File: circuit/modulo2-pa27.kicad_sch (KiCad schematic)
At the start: 47 parts, among them J2 CONN_01X04, J3 CONN_01X04, J4 JACK_MONO, J5 HOLE, J7 HOLE, SW1 bright, U1 OPA2134, U2 OPA2134, U3 TLE2426

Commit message: further routing
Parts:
- C10, C4: footprint myAmp:C_FILM_L7.2mm_W3.5mm_P5.00mm -> myAmp:C_2.5MM
- C22, C23: footprint myAmp:C_1206 -> myAmp:C_5MM_1206
- C5: value 1n -> 250p
- C6: value 220n -> 100n
- C7: value 100n -> 47n
- R8: value 33k -> 100k
- RV1, RV2: value 50k -> 250k
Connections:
- net TRB: now also C5.2, RV1.3; no longer RV1.2, RV4.3
- new net: RV1.2, RV4.3
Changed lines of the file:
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@@
     (effects (font (size 1.27 1.27)) (justify left bottom))
   )
-  (label "TRB" (at 134.62 41.91 0)
+  (label "TRB" (at 123.19 34.29 0)
     (effects (font (size 1.27 1.27)) (justify left bottom))
   )
@@
     (property "Reference" "C22" (id 0) (at 16.51 69.85 0))
     (property "Value" "100nF" (id 1) (at 15.24 64.77 0))
-    (property "Footprint" "myAmp:C_1206" (id 2) (at 18.0848 63.5 0)
+    (property "Footprint" "myAmp:C_5MM_1206" (id 2) (at 18.0848 63.5 0)
       (effects (font (size 1.27 1.27)) hide)
     )
@@
       (effects (font (size 1.27 1.27)) (justify right))
     )
-    (property "Value" "50k" (id 1) (at 125.222 43.053 0)
+    (property "Value" "250k" (id 1) (at 125.222 43.053 0)
       (effects (font (size 1.27 1.27)) (justify right))
     )
@@
       (effects (font (size 1.27 1.27)) (justify right))
     )
-    (property "Value" "50k" (id 1) (at 125.222 58.293 0)
+    (property "Value" "250k" (id 1) (at 125.222 58.293 0)
       (effects (font (size 1.27 1.27)) (justify right))
     )
@@
     (in_bom yes) (on_board yes)
     (property "Reference" "C5" (id 0) (at 118.11 30.48 90))
-    (property "Value" "1n" (id 1) (at 118.11 38.1 90))
+    (property "Value" "250p" (id 1) (at 118.11 38.1 90))
     (property "Footprint" "myAmp:C_FILM_L7.2mm_W3.5mm_P5.00mm" (id 2) (at 121.92 33.3248 0)
       (effects (font (size 1.27 1.27)) hide)
@@
       (effects (font (size 1.27 1.27)) (justify right))
     )
-    (property "Value" "33k" (id 1) (at 110.49 43.18 0)
+    (property "Value" "100k" (id 1) (at 110.49 43.18 0)
       (effects (font (size 1.27 1.27)) (justify right))
     )
@@
   (symbol (lib_id "myAmp:C") (at 118.11 49.53 90) (unit 1)
     (in_bom yes) (on_board yes)
-    (property "Reference" "C6" (id 0) (at 118.11 46.99 90))
-    (property "Value" "220n" (id 1) (at 118.11 53.34 90))
+    (property "Reference" "C6" (id 0) (at 118.11 45.72 90))
+    (property "Value" "100n" (id 1) (at 118.11 53.34 90))
     (property "Footprint" "myAmp:C_FILM_L7.2mm_W3.5mm_P5.00mm" (id 2) (at 121.92 48.5648 0)
       (effects (font (size 1.27 1.27)) hide)
@@
   (symbol (lib_id "myAmp:C") (at 118.11 63.5 90) (unit 1)
     (in_bom yes) (on_board yes)
-    (property "Reference" "C7" (id 0) (at 118.11 60.96 90))
-    (property "Value" "100n" (id 1) (at 118.11 67.31 90))
+    (property "Reference" "C7" (id 0) (at 118.11 59.69 90))
+    (property "Value" "47n" (id 1) (at 118.11 67.31 90))
     (property "Footprint" "myAmp:C_FILM_L7.2mm_W3.5mm_P5.00mm" (id 2) (at 121.92 62.5348 0)
       (effects (font (size 1.27 1.27)) hide)
@@
     (property "Reference" "C10" (id 0) (at 179.07 53.34 90))
     (property "Value" "120p" (id 1) (at 179.07 60.96 90))
-    (property "Footprint" "myAmp:C_FILM_L7.2mm_W3.5mm_P5.00mm" (id 2) (at 182.88 56.1848 0)
+    (property "Footprint" "myAmp:C_2.5MM" (id 2) (at 182.88 56.1848 0)
       (effects (font (size 1.27 1.27)) hide)
     )
@@
     (property "Reference" "C4" (id 0) (at 99.06 53.34 90))
     (property "Value" "120p" (id 1) (at 99.06 60.96 90))
-    (property "Footprint" "myAmp:C_FILM_L7.2mm_W3.5mm_P5.00mm" (id 2) (at 102.87 56.1848 0)
+    (property "Footprint" "myAmp:C_2.5MM" (id 2) (at 102.87 56.1848 0)
       (effects (font (size 1.27 1.27)) hide)
     )
@@
     (property "Reference" "C23" (id 0) (at 36.83 69.85 0))
     (property "Value" "100nF" (id 1) (at 35.56 64.77 0))
-    (property "Footprint" "myAmp:C_1206" (id 2) (at 38.4048 63.5 0)
+    (property "Footprint" "myAmp:C_5MM_1206" (id 2) (at 38.4048 63.5 0)
       (effects (font (size 1.27 1.27)) hide)
     )
@@
     )
     (path "/48142eaa-7210-4390-91e8-e59685a2b4d4"
-      (reference "C4") (unit 1) (value "120p") (footprint "myAmp:C_FILM_L7.2mm_W3.5mm_P5.00mm")
+      (reference "C4") (unit 1) (value "120p") (footprint "myAmp:C_2.5MM")
     )
     (path "/00000000-0000-0000-0000-000061c307c0"
-      (reference "C5") (unit 1) (value "1n") (footprint "myAmp:C_FILM_L7.2mm_W3.5mm_P5.00mm")
+      (reference "C5") (unit 1) (value "250p") (footprint "myAmp:C_FILM_L7.2mm_W3.5mm_P5.00mm")
     )
     (path "/00000000-0000-0000-0000-000061c52359"
-      (reference "C6") (unit 1) (value "220n") (footprint "myAmp:C_FILM_L7.2mm_W3.5mm_P5.00mm")
+      (reference "C6") (unit 1) (value "100n") (footprint "myAmp:C_FILM_L7.2mm_W3.5mm_P5.00mm")
     )
     (path "/00000000-0000-0000-0000-000061c52e5e"
-      (reference "C7") (unit 1) (value "100n") (footprint "myAmp:C_FILM_L7.2mm_W3.5mm_P5.00mm")
+      (reference "C7") (unit 1) (value "47n") (footprint "myAmp:C_FILM_L7.2mm_W3.5mm_P5.00mm")
     )
     (path "/11af6226-d94c-469b-95d8-d952d2567f76"
@@
     )
     (path "/1c4bff62-038b-4006-b722-9d6b6553e13a"
-      (reference "C10") (unit 1) (value "120p") (footprint "myAmp:C_FILM_L7.2mm_W3.5mm_P5.00mm")
+      (reference "C10") (unit 1) (value "120p") (footprint "myAmp:C_2.5MM")
     )
     (path "/70af284c-9682-4272-9658-52b4c38f7d80"
@@
     )
     (path "/00000000-0000-0000-0000-00005f0669ed"
-      (reference "C22") (unit 1) (value "100nF") (footprint "myAmp:C_1206")
+      (reference "C22") (unit 1) (value "100nF") (footprint "myAmp:C_5MM_1206")
     )
     (path "/fb1c6638-be6b-421d-993a-23927fb374fb"
-      (reference "C23") (unit 1) (value "100nF") (footprint "myAmp:C_1206")
+      (reference "C23") (unit 1) (value "100nF") (footprint "myAmp:C_5MM_1206")
     )
     (path "/00000000-0000-0000-0000-000061b9e69a"
@@
     )
     (path "/00000000-0000-0000-0000-000061c471ae"
-      (reference "R8") (unit 1) (value "33k") (footprint "myAmp:R_10MM")
+      (reference "R8") (unit 1) (value "100k") (footprint "myAmp:R_10MM")
     )
     (path "/844c38d0-9f18-4b6e-9f2e-f1c5539e0fd4"
@@
     )
     (path "/00000000-0000-0000-0000-000061c2ed9a"
-      (reference "RV1") (unit 1) (value "50k") (footprint "myAmp:BOURNS_PTD901_xx15K")
+      (reference "RV1") (unit 1) (value "250k") (footprint "myAmp:BOURNS_PTD901_xx15K")
     )
     (path "/00000000-0000-0000-0000-000061c2f7c7"
-      (reference "RV2") (unit 1) (value "50k") (footprint "myAmp:BOURNS_PTD901_xx15K")
+      (reference "RV2") (unit 1) (value "250k") (footprint "myAmp:BOURNS_PTD901_xx15K")
     )
     (path "/00000000-0000-0000-0000-000061c300fc"

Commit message: redone layout and tracing
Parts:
- added C24, C25: 47u, myAmp:CPOL_D6.3_P2.5, symbol myAmp:CPOL
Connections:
- net +24V: now also C24.1, C25.1
- net GND: now also C24.2, C25.2
- net PA_OUT: now also J3.2 (P2), J3.4; no longer J3.1 (P1), J3.3
- net VGND: now also J3.1 (P1), J3.3; no longer J3.2 (P2), J3.4
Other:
- moved on the sheet: J3
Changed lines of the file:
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@@
   (junction (at 109.22 34.29) (diameter 0) (color 0 0 0 0)
   )
+  (junction (at 102.87 102.87) (diameter 0) (color 0 0 0 0)
+  )
   (junction (at 44.45 57.15) (diameter 0) (color 0 0 0 0)
   )
   (junction (at 127 63.5) (diameter 0) (color 0 0 0 0)
+  )
+  (junction (at 78.74 176.53) (diameter 0) (color 0 0 0 0)
   )
   (junction (at 161.29 48.26) (diameter 0) (color 0 0 0 0)
@@
     (stroke (width 0) (type default) (color 0 0 0 0))
   )
-  (wire (pts (xy 50.8 182.88) (xy 58.42 182.88))
+  (wire (pts (xy 50.8 172.72) (xy 58.42 172.72))
     (stroke (width 0) (type default) (color 0 0 0 0))
   )
@@
     (stroke (width 0) (type default) (color 0 0 0 0))
   )
+  (wire (pts (xy 78.74 182.88) (xy 78.74 185.42))
+    (stroke (width 0) (type default) (color 0 0 0 0))
+  )
   (wire (pts (xy 200.66 54.61) (xy 200.66 59.69))
     (stroke (width 0) (type default) (color 0 0 0 0))
@@
     (stroke (width 0) (type default) (color 0 0 0 0))
   )
+  (wire (pts (xy 102.87 102.87) (xy 102.87 105.41))
+    (stroke (width 0) (type default) (color 0 0 0 0))
+  )
   (wire (pts (xy 184.15 57.15) (xy 181.61 57.15))
     (stroke (width 0) (type default) (color 0 0 0 0))
@@
     (stroke (width 0) (type default) (color 0 0 0 0))
   )
+  (wire (pts (xy 78.74 176.53) (xy 78.74 177.8))
+    (stroke (width 0) (type default) (color 0 0 0 0))
+  )
   (wire (pts (xy 80.01 44.45) (xy 82.55 44.45))
     (stroke (width 0) (type default) (color 0 0 0 0))
@@
   )
   (wire (pts (xy 193.04 54.61) (xy 200.66 54.61))
+    (stroke (width 0) (type default) (color 0 0 0 0))
+  )
+  (wire (pts (xy 102.87 110.49) (xy 102.87 114.3))
     (stroke (width 0) (type default) (color 0 0 0 0))
   )
@@
     (effects (font (size 1.27 1.27)) (justify left bottom))
   )
-  (label "VGND" (at 50.8 182.88 0)
+  (label "VGND" (at 50.8 172.72 0)
     (effects (font (size 1.27 1.27)) (justify left bottom))
   )
@@
     (pin "1")
   )
-  (symbol (lib_id "myAmp:CONN_01X04") (at 63.5 179.07 0) (unit 1)
-    (in_bom yes) (on_board yes)
-    (property "Reference" "J3" (id 0) (at 65.4812 179.197 0)
+  (symbol (lib_id "myAmp:CONN_01X04") (at 63.5 176.53 0) (unit 1)
+    (in_bom yes) (on_board yes)
+    (property "Reference" "J3" (id 0) (at 65.4812 176.657 0)
       (effects (font (size 1.27 1.27)) (justify left))
     )
-    (property "Value" "CONN_01X04" (id 1) (at 66.04 179.07 90)
-      (effects (font (size 1.27 1.27)) hide)
-    )
-    (property "Footprint" "myAmp:PIN_1x04" (id 2) (at 63.5 179.07 0)
-      (effects (font (size 1.27 1.27)) hide)
-    )
-    (property "Datasheet" "" (id 3) (at 63.5 179.07 0)
+    (property "Value" "CONN_01X04" (id 1) (at 66.04 176.53 90)
+      (effects (font (size 1.27 1.27)) hide)
+    )
+    (property "Footprint" "myAmp:PIN_1x04" (id 2) (at 63.5 176.53 0)
+      (effects (font (size 1.27 1.27)) hide)
+    )
+    (property "Datasheet" "" (id 3) (at 63.5 176.53 0)
       (effects (font (size 1.27 1.27)) hide)
     )
@@
     (pin "2")
   )
+  (symbol (lib_id "myAmp:CPOL") (at 78.74 180.34 0) (unit 1)
+    (in_bom yes) (on_board yes) (fields_autoplaced)
+    (property "Reference" "C24" (id 0) (at 81.28 178.5238 0)
+      (effects (font (size 1.27 1.27)) (justify left))
+    )
+    (property "Value" "47u" (id 1) (at 81.28 181.0638 0)
+      (effects (font (size 1.27 1.27)) (justify left))
+    )
+    (property "Footprint" "myAmp:CPOL_D6.3_P2.5" (id 2) (at 78.74 180.34 0)
+      (effects (font (size 1.27 1.27)) hide)
+    )
+    (property "Datasheet" "" (id 3) (at 78.74 180.34 0)
+      (effects (font (size 1.27 1.27)) hide)
+    )
+    (pin "1")
+    (pin "2")
+  )
   (symbol (lib_id "myAmp:C") (at 179.07 57.15 90) (unit 1)
     (in_bom yes) (on_board yes)
@@
     (pin "2")
   )
+  (symbol (lib_id "power:GND") (at 102.87 114.3 0) (unit 1)
+    (in_bom yes) (on_board yes)
+    (property "Reference" "#PWR0101" (id 0) (at 102.87 120.65 0)
+      (effects (font (size 1.27 1.27)) hide)
+    )
+    (property "Value" "GND" (id 1) (at 102.997 118.6942 0))
+    (property "Footprint" "" (id 2) (at 102.87 114.3 0)
+      (effects (font (size 1.27 1.27)) hide)
+    )
+    (property "Datasheet" "" (id 3) (at 102.87 114.3 0)
+      (effects (font (size 1.27 1.27)) hide)
+    )
+    (pin "1")
+  )
   (symbol (lib_id "myAmp:R") (at 236.22 63.5 180) (unit 1)
     (in_bom yes) (on_board yes)
@@
     (pin "1")
     (pin "2")
+  )
+  (symbol (lib_id "power:GND") (at 78.74 185.42 0) (mirror y) (unit 1)
+    (in_bom yes) (on_board yes)
+    (property "Reference" "#PWR03" (id 0) (at 78.74 191.77 0)
+      (effects (font (size 1.27 1.27)) hide)
+    )
+    (property "Value" "GND" (id 1) (at 78.613 189.8142 0))
+    (property "Footprint" "" (id 2) (at 78.74 185.42 0)
+      (effects (font (size 1.27 1.27)) hide)
+    )
+    (property "Datasheet" "" (id 3) (at 78.74 185.42 0)
+      (effects (font (size 1.27 1.27)) hide)
+    )
+    (pin "1")
   )
   (symbol (lib_id "myAmp:OPAMP") (at 250.19 39.37 0) (unit 2)
@@
     (pin "3")
   )
+  (symbol (lib_id "myAmp:CPOL") (at 102.87 107.95 0) (unit 1)
+    (in_bom yes) (on_board yes) (fields_autoplaced)
+    (property "Reference" "C25" (id 0) (at 105.41 106.1338 0)
+      (effects (font (size 1.27 1.27)) (justify left))
+    )
+    (property "Value" "47u" (id 1) (at 105.41 108.6738 0)
+      (effects (font (size 1.27 1.27)) (justify left))
+    )
+    (property "Footprint" "myAmp:CPOL_D6.3_P2.5" (id 2) (at 102.87 107.95 0)
+      (effects (font (size 1.27 1.27)) hide)
+    )
+    (property "Datasheet" "" (id 3) (at 102.87 107.95 0)
+      (effects (font (size 1.27 1.27)) hide)
+    )
+    (pin "1")
+    (pin "2")
+  )
   (symbol (lib_id "myAmp:R") (at 241.3 63.5 0) (mirror x) (unit 1)
     (in_bom yes) (on_board yes)
@@
       (reference "#PWR02") (unit 1) (value "+24V") (footprint "")
     )
+    (path "/90800a4d-a014-4b9a-947e-f975697802ee"
+      (reference "#PWR03") (unit 1) (value "GND") (footprint "")
+    )
     (path "/00000000-0000-0000-0000-00005f0669e6"
       (reference "#PWR05") (unit 1) (value "GND") (footprint "")
@@
       (reference "#PWR012") (unit 1) (value "GND") (footprint "")
     )
+    (path "/84916f83-d8a0-446a-8998-d523c09d50ab"
+      (reference "#PWR0101") (unit 1) (value "GND") (footprint "")
+    )
     (path "/00000000-0000-0000-0000-000061baa65d"
       (reference "C1") (unit 1) (value "47nF") (footprint "myAmp:C_FILM_L7.2mm_W3.5mm_P5.00mm")
@@
       (reference "C23") (unit 1) (value "100nF") (footprint "myAmp:C_5MM_1206")
     )
+    (path "/193e6f89-e90a-407b-9332-2aace38b0407"
+      (reference "C24") (unit 1) (value "47u") (footprint "myAmp:CPOL_D6.3_P2.5")
+    )
+    (path "/bec0516f-9815-4d8e-ba32-5bcb5afe996f"
+      (reference "C25") (unit 1) (value "47u") (footprint "myAmp:CPOL_D6.3_P2.5")
+    )
     (path "/00000000-0000-0000-0000-000061b9e69a"

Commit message: made a toner transfer pa27
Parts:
- RV4: footprint myAmp:BOURNS_PTD901_xx15K -> myAmp:POT_VULGARIS
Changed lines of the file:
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@@
       (effects (font (size 1.27 1.27)) (justify right))
     )
-    (property "Footprint" "myAmp:BOURNS_PTD901_xx15K" (id 2) (at 144.78 48.26 0)
+    (property "Footprint" "myAmp:POT_VULGARIS" (id 2) (at 144.78 48.26 0)
       (effects (font (size 1.27 1.27)) hide)
     )
@@
     )
     (path "/3815e89f-ae0b-444f-8039-7f1b98ab98ab"
-      (reference "RV4") (unit 1) (value "500k") (footprint "myAmp:BOURNS_PTD901_xx15K")
+      (reference "RV4") (unit 1) (value "500k") (footprint "myAmp:POT_VULGARIS")
     )
     (path "/77415905-9ad6-47f9-b33e-2e8f06373b35"

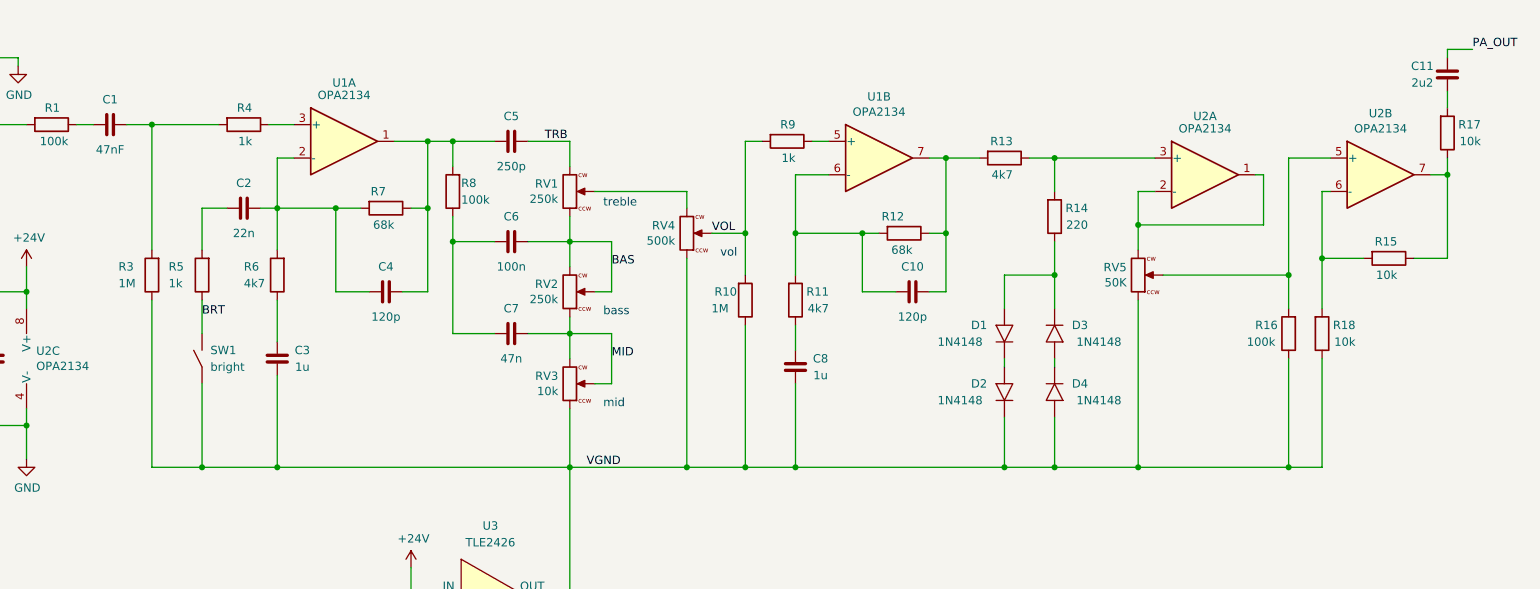
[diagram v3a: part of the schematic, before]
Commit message: made FV-1 prototype; converted kicad 5 files to kicad 6
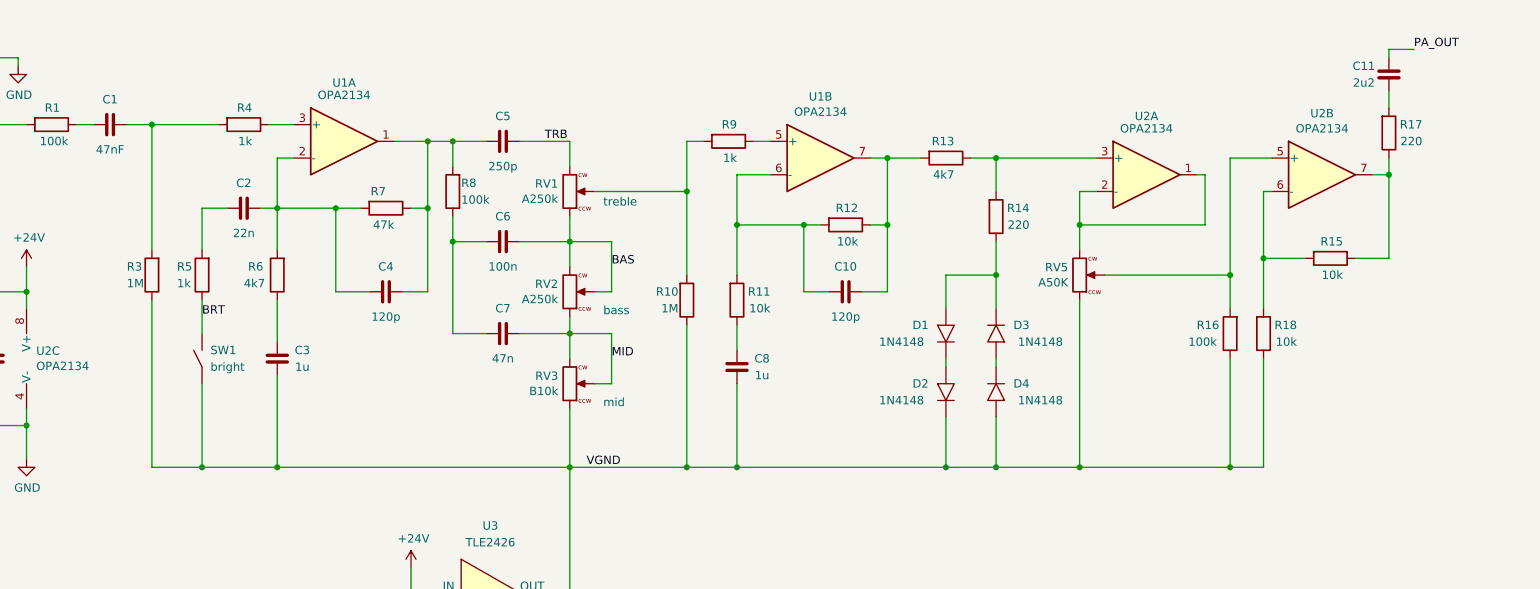
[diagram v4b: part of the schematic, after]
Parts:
- removed RV4: 500k, myAmp:POT_VULGARIS, symbol myAmp:R_POT
- R11: value 4k7 -> 10k
- R12: value 68k -> 10k
- R17: value 10k -> 220
- R7: value 68k -> 47k
- RV1, RV2: value 250k -> A250k
- RV3: value 10k -> B10k
- RV5: value 50K -> A50K
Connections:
- net VOL is gone; now on an unnamed net: R10.2, R9.2
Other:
- note removed: "vol"
- moved on the sheet: C10, C11, C5, C6, C7, C8, D1, D2, D3, D4, R10, R11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
